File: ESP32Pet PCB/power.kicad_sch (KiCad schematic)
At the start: 5 parts, among them J1 3.7V LIPO, U1 3.3V LDO, U3 TP4057

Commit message: Schematic Updated
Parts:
- removed C1: 10uF, SparkFun-Capacitor:C_0603_1608Metric, symbol SparkFun-Capacitor:C
- removed C2: 0.1uF, Capacitor_SMD:C_1808_4520Metric_Pad1.72x2.30mm_HandSolder, symbol SparkFun-Capacitor:C
- removed J1: 3.7V LIPO, SparkFun-Connector:JST_SMD_2.0mm-2, symbol SparkFun-Connector:Conn_01x02_JST_2.0mm_LiPo
- removed U3: TP4057, Package_TO_SOT_SMD:TSOT-23-6, symbol Battery_Management:TP4057
- added C1: 10 uF, Capacitor_THT:CP_Radial_D4.0mm_P1.50mm, symbol Device:C
- added J2: 3.7V LIPO + CHARGING, Connector_PinSocket_1.00mm:PinSocket_1x02_P1.00mm_Vertical, symbol Connector:Conn_01x02_Socket
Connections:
- net GND: now also C1.1, J2.2 (Pin_2); no longer U1.3 (VO)
- net LIPO+: no longer names the net of U1.2 (VI)
- net LIPO+: now also C1.2, J2.1 (Pin_1)
- new net 3.3V: U1.3 (VO)
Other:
- note removed: "Decoupling Capacitors"
- note removed: "Update TP4057 (HiLetGo TP4057 USB-C Battery Manager)"

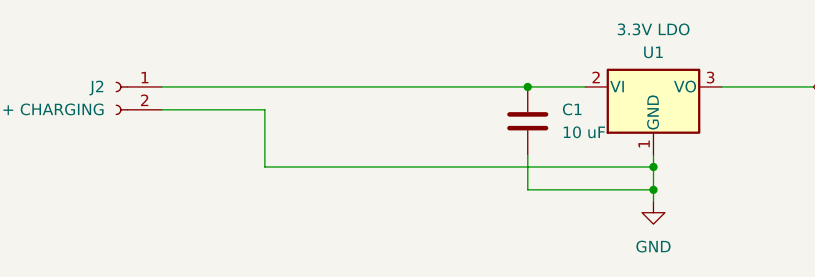
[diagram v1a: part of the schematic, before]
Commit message: Schematic complete, created custom footprints and symbols for TFT LCD
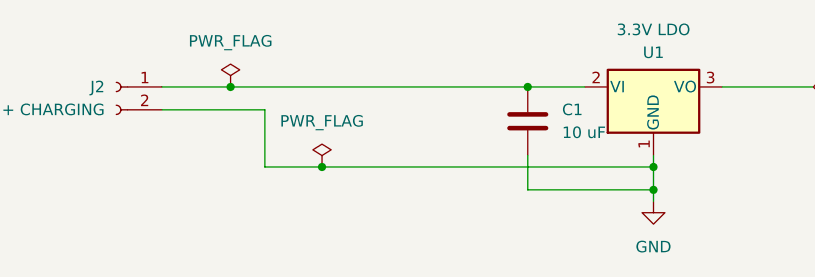
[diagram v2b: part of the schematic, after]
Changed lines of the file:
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@@
+	)
+	(junction
+		(at 74.93 58.42)
+		(diameter 0)
+		(color 0 0 0 0)
 	)
 	(junction
@@
 		(color 0 0 0 0)
 	)
+	(junction
+		(at 85.09 67.31)
+		(diameter 0)
+		(color 0 0 0 0)
+	)
 	(wire
 		(pts
@@
 	(wire
 		(pts
-			(xy 78.74 67.31) (xy 121.92 67.31)
+			(xy 78.74 67.31) (xy 85.09 67.31)
 		)
 		(stroke
@@
 	(wire
 		(pts
+			(xy 74.93 58.42) (xy 107.95 58.42)
+		)
+		(stroke
+			(width 0)
+			(type default)
+		)
+	)
+	(wire
+		(pts
 			(xy 121.92 67.31) (xy 121.92 69.85)
 		)
@@
 	(wire
 		(pts
+			(xy 85.09 67.31) (xy 121.92 67.31)
+		)
+		(stroke
+			(width 0)
+			(type default)
+		)
+	)
+	(wire
+		(pts
 			(xy 107.95 69.85) (xy 121.92 69.85)
 		)
@@
 	(wire
 		(pts
-			(xy 67.31 58.42) (xy 107.95 58.42)
+			(xy 67.31 58.42) (xy 74.93 58.42)
 		)
 		(stroke
@@
 				(justify left)
 				(hide yes)
+			)
+		)
+	)
+	(symbol
+		(lib_id "power:PWR_FLAG")
+		(at 74.93 58.42 0)
+		(unit 1)
+		(exclude_from_sim no)
+		(in_bom yes)
+		(on_board yes)
+		(dnp no)
+		(fields_autoplaced yes)
+		(property "Reference" "#FLG01"
+			(at 74.93 56.515 0)
+			(effects
+				(font
+					(size 1.27 1.27)
+				)
+				(hide yes)
+			)
+		)
+		(property "Value" "PWR_FLAG"
+			(at 74.93 53.34 0)
+			(effects
+				(font
+					(size 1.27 1.27)
+				)
+			)
+		)
+		(property "Footprint" ""
+			(at 74.93 58.42 0)
+			(effects
+				(font
+					(size 1.27 1.27)
+				)
+				(hide yes)
+			)
+		)
+		(property "Datasheet" "~"
+			(at 74.93 58.42 0)
+			(effects
+				(font
+					(size 1.27 1.27)
+				)
+				(hide yes)
+			)
+		)
+		(property "Description" "Special symbol for telling ERC where power comes from"
+			(at 74.93 58.42 0)
+			(effects
+				(font
+					(size 1.27 1.27)
+				)
+				(hide yes)
+			)
+		)
+		(pin "1"
+		)
+		(instances
+			(project "ESP32Pet"
+				(path "/397abc7c-300b-4d6f-9337-33290484b5ae/96da55df-4a44-41f7-a6e8-307058d63992"
+					(reference "#FLG01")
+					(unit 1)
+				)
 			)
 		)
@@
 					(unit 1)
 				)
+			)
+		)
+	)
+	(symbol
+		(lib_id "power:PWR_FLAG")
+		(at 85.09 67.31 0)
+		(unit 1)
+		(exclude_from_sim no)
+		(in_bom yes)
+		(on_board yes)
+		(dnp no)
+		(fields_autoplaced yes)
+		(property "Reference" "#FLG02"
+			(at 85.09 65.405 0)
+			(effects
+				(font
+					(size 1.27 1.27)
+				)
+				(hide yes)
+			)
+		)
+		(property "Value" "PWR_FLAG"
+			(at 85.09 62.23 0)
+			(effects
+				(font
+					(size 1.27 1.27)
+				)
+			)
+		)
+		(property "Footprint" ""
+			(at 85.09 67.31 0)
+			(effects
+				(font
+					(size 1.27 1.27)
+				)
+				(hide yes)
+			)
+		)
+		(property "Datasheet" "~"
+			(at 85.09 67.31 0)
+			(effects
+				(font
+					(size 1.27 1.27)
+				)
+				(hide yes)
+			)
+		)
+		(property "Description" "Special symbol for telling ERC where power comes from"
+			(at 85.09 67.31 0)
+			(effects
+				(font
+					(size 1.27 1.27)
+				)
+				(hide yes)
+			)
+		)
+		(pin "1"
+		)
+		(instances
+			(project "ESP32Pet"
+				(path "/397abc7c-300b-4d6f-9337-33290484b5ae/96da55df-4a44-41f7-a6e8-307058d63992"
+					(reference "#FLG02")
+					(unit 1)
+				)

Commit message: PCB Design Complete
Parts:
- J2: footprint Connector_PinSocket_1.00mm:PinSocket_1x02_P1.00mm_Vertical -> Connector_PinHeader_2.54mm:PinHeader_1x02_P2.54mm_Vertical
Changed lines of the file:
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@@
 			)
 		)
-		(property "Footprint" "Connector_PinSocket_1.00mm:PinSocket_1x02_P1.00mm_Vertical"
+		(property "Footprint" "Connector_PinHeader_2.54mm:PinHeader_1x02_P2.54mm_Vertical"
 			(at 62.23 58.42 0)
 			(effects
